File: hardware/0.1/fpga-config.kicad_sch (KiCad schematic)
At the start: 31 parts, among them J2 JTAG, J5 USB_C_Receptacle_USB2.0, Q1 BSS138, SW1 SW_Push, U1 ECP5U_12_CABGA256, U4 USBLC6-2SC6, U6 W25Q128JVSIQ

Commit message: all DRC / ERC errors signed off
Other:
- note added: "Enables bootloader to reset into user land. DNP until bootloader development begins."
- note added: "IO / configure to jump to bootloader"
- note removed: "Can be used for IO or to jump to bootloader"
- note removed: "Self reboot system? DNP until I figure out what goes on."
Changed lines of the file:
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@@
   (page 3 5)
   (paper "A4")
+  (bus_alias "CONFIG" (members "CFG_CLK" "CFG_IO[0..3]" "CFG_CDONE" "CFG_CS"))
   (junction (at 27.305 74.93) (diameter 1.016) (color 0 0 0 0))
+  (junction (at 46.99 35.56) (diameter 1.016) (color 0 0 0 0))
   (junction (at 47.625 49.53) (diameter 1.016) (color 0 0 0 0))
   (junction (at 47.625 54.61) (diameter 1.016) (color 0 0 0 0))
@@
   (junction (at 269.24 57.15) (diameter 1.016) (color 0 0 0 0))
   (junction (at 269.24 71.12) (diameter 1.016) (color 0 0 0 0))
-  (no_connect (at 229.87 111.76))
-  (no_connect (at 46.355 66.04))
-  (no_connect (at 229.87 144.78))
-  (no_connect (at 46.355 63.5))
+  (no_connect (at 229.87 121.92))
   (no_connect (at 229.87 119.38))
   (no_connect (at 229.87 114.3))
   (no_connect (at 229.87 116.84))
+  (no_connect (at 46.355 63.5))
+  (no_connect (at 229.87 111.76))
+  (no_connect (at 46.355 66.04))
   (no_connect (at 229.87 137.16))
-  (no_connect (at 229.87 121.92))
+  (no_connect (at 229.87 144.78))
   (bus_entry (at 114.935 49.53) (size 2.54 -2.54)
     (stroke (width 0.1524) (type solid) (color 0 0 0 0))
@@
     (stroke (width 0) (type solid) (color 0 0 0 0))
   )
-  (wire (pts (xy 46.355 35.56) (xy 48.895 35.56))
+  (wire (pts (xy 46.355 35.56) (xy 46.99 35.56))
     (stroke (width 0) (type solid) (color 0 0 0 0))
   )
@@
   )
   (wire (pts (xy 46.355 55.88) (xy 47.625 55.88))
+    (stroke (width 0) (type solid) (color 0 0 0 0))
+  )
+  (wire (pts (xy 46.99 30.48) (xy 46.99 35.56))
+    (stroke (width 0) (type solid) (color 0 0 0 0))
+  )
+  (wire (pts (xy 46.99 35.56) (xy 48.895 35.56))
     (stroke (width 0) (type solid) (color 0 0 0 0))
   )
@@
     (effects (font (size 5 5)) (justify right bottom))
   )
-  (text "Can be used for IO or\nto jump to bootloader" (at 162.56 153.67 180)
+  (text "IO / configure to \njump to bootloader" (at 162.56 153.67 180)
     (effects (font (size 1.27 1.27)) (justify right bottom))
   )
@@
     (effects (font (size 1.27 1.27)) (justify left bottom))
   )
-  (text "Self reboot system?\nDNP until I figure out what goes on."
-    (at 198.12 153.67 0)
+  (text "Enables bootloader to reset into user land.\nDNP until bootloader development begins."
+    (at 200.66 154.94 0)
     (effects (font (size 1.27 1.27)) (justify left bottom))
   )
@@
     (effects (font (size 1.27 1.27)) (justify left bottom))
   )
+  (label "{CONFIG}" (at 215.9 45.72 270)
+    (effects (font (size 1.27 1.27)) (justify right bottom))
+  )
   (label "CFG_CLK" (at 218.44 99.06 0)
     (effects (font (size 1.27 1.27)) (justify left bottom))
@@
     (effects (font (size 1.27 1.27)) (justify left))
   )
+  (symbol (lib_id "power:PWR_FLAG") (at 46.99 30.48 0) (unit 1)
+    (in_bom yes) (on_board yes)
+    (property "Reference" "#FLG0105" (id 0) (at 46.99 28.575 0)
+      (effects (font (size 1.27 1.27)) hide)
+    )
+    (property "Value" "PWR_FLAG" (id 1) (at 46.99 26.67 0))
+    (property "Footprint" "" (id 2) (at 46.99 30.48 0)
+      (effects (font (size 1.27 1.27)) hide)
+    )
+    (property "Datasheet" "~" (id 3) (at 46.99 30.48 0)
+      (effects (font (size 1.27 1.27)) hide)
+    )
+  )
   (symbol (lib_id "power:+3V3") (at 24.13 97.79 0) (mirror y) (unit 1)

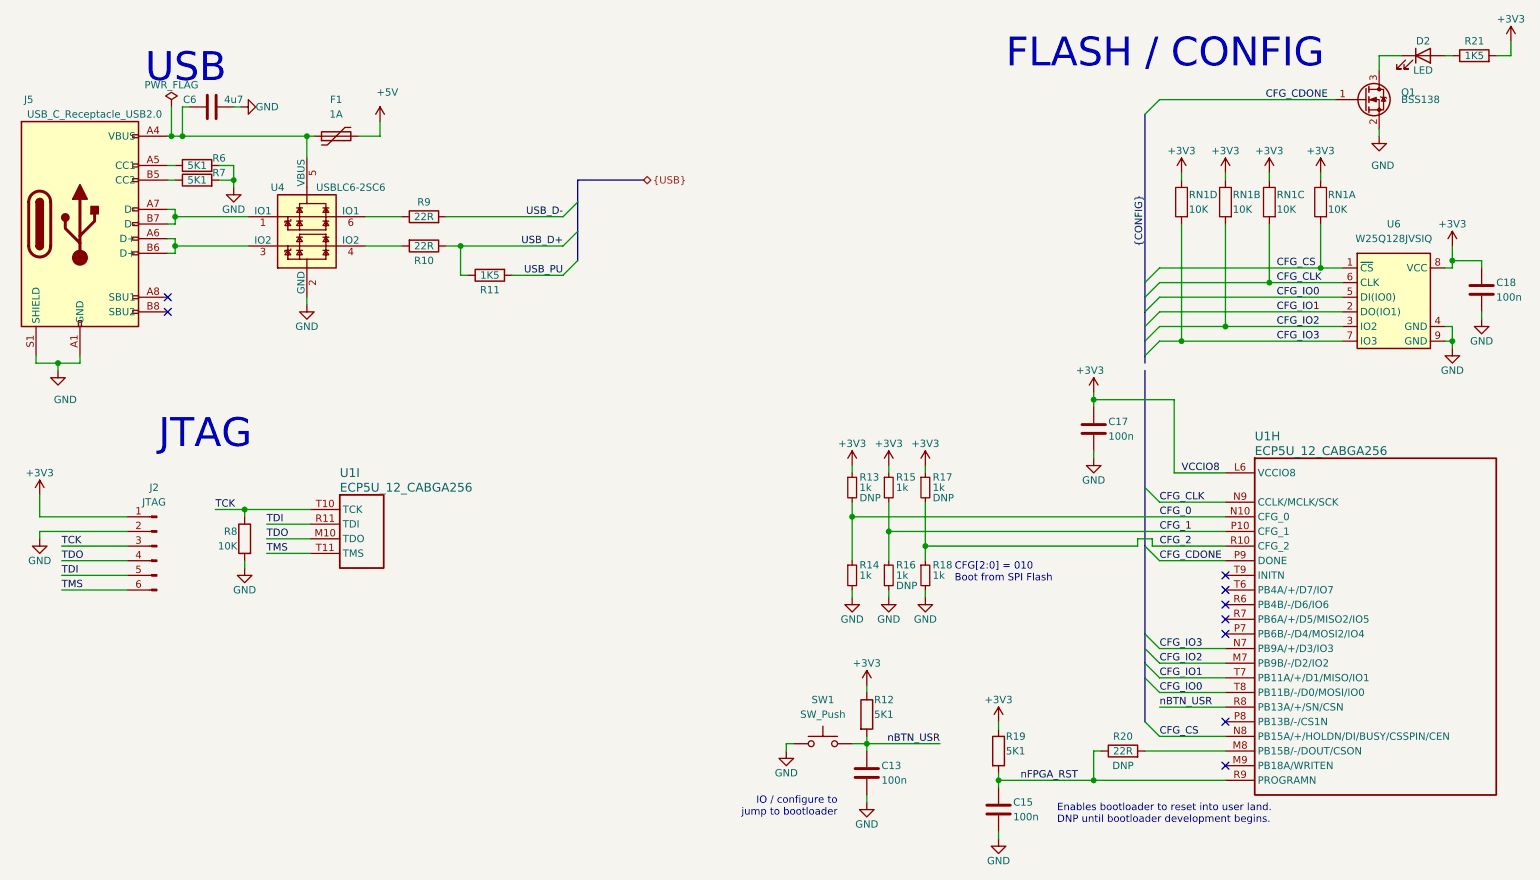
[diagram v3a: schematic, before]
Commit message: adding silk
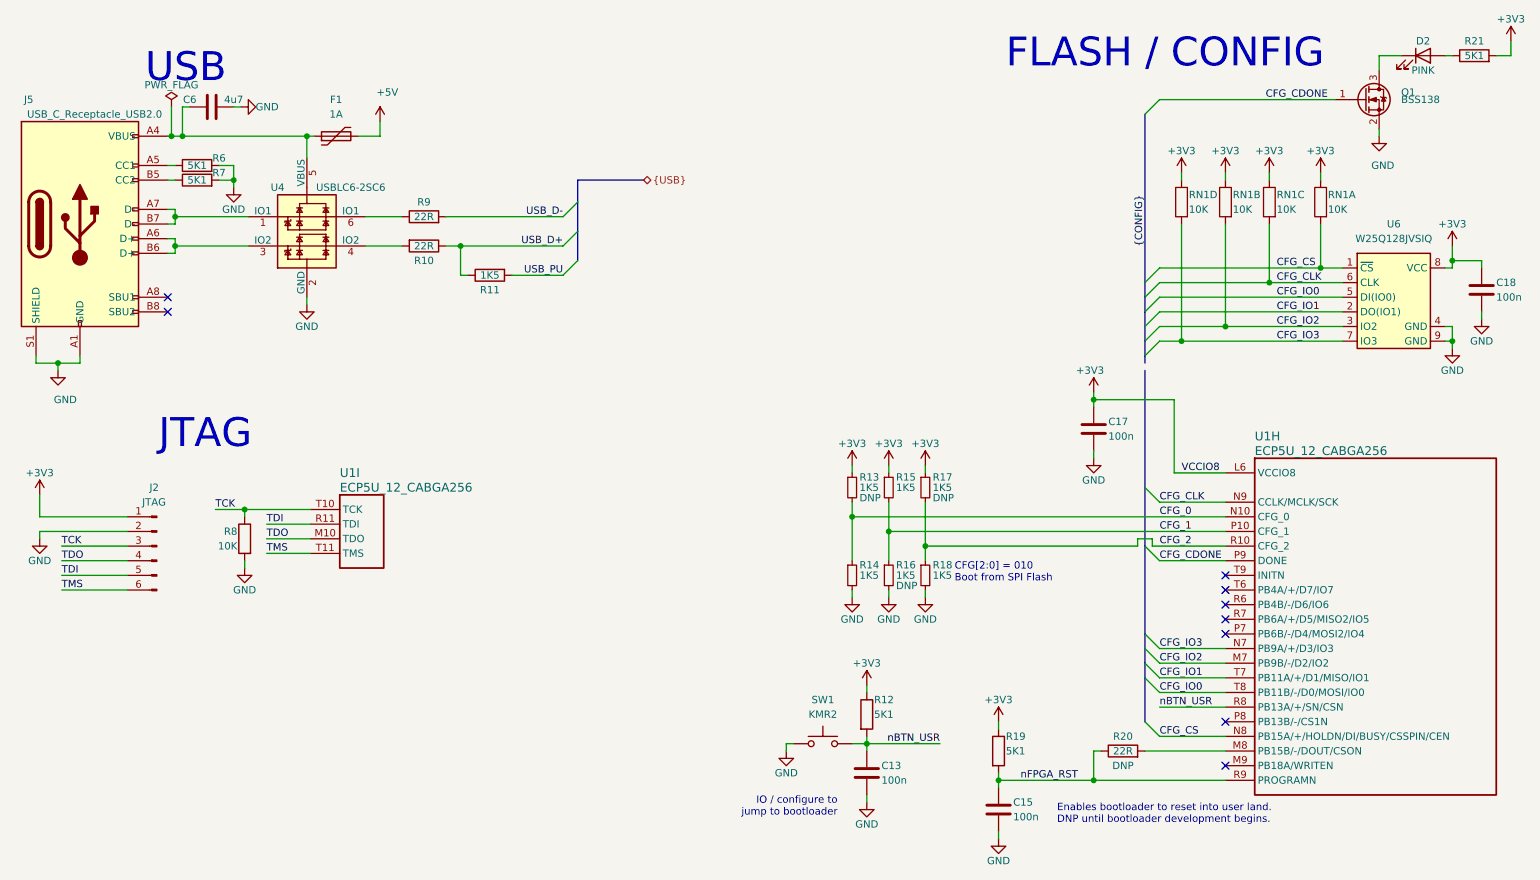
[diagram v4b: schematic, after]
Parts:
- D2: value LED -> PINK
- J2: DNP (none) -> DNP
- R13, R14, R15, R16, R17, R18: value 1k -> 1K5
- R21: value 1K5 -> 5K1
- SW1: value SW_Push -> KMR2
- U1: manf# ECP5U_12 -> (none)
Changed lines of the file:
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@@
   (junction (at 269.24 57.15) (diameter 1.016) (color 0 0 0 0))
   (junction (at 269.24 71.12) (diameter 1.016) (color 0 0 0 0))
+  (no_connect (at 229.87 121.92))
   (no_connect (at 229.87 111.76))
-  (no_connect (at 229.87 121.92))
-  (no_connect (at 229.87 116.84))
+  (no_connect (at 229.87 144.78))
   (no_connect (at 46.355 63.5))
   (no_connect (at 229.87 114.3))
+  (no_connect (at 229.87 119.38))
+  (no_connect (at 229.87 116.84))
+  (no_connect (at 46.355 66.04))
   (no_connect (at 229.87 137.16))
-  (no_connect (at 229.87 144.78))
-  (no_connect (at 46.355 66.04))
-  (no_connect (at 229.87 119.38))
   (bus_entry (at 114.935 49.53) (size 2.54 -2.54)
     (stroke (width 0.1524) (type solid) (color 0 0 0 0))
@@
       (effects (font (size 1.27 1.27)) (justify left top))
     )
-    (property "Value" "1k" (id 1) (at 166.37 96.52 0)
+    (property "Value" "1K5" (id 1) (at 166.37 96.52 0)
       (effects (font (size 1.27 1.27)) (justify left))
     )
@@
       (effects (font (size 1.27 1.27)) (justify left top))
     )
-    (property "Value" "1k" (id 1) (at 166.37 111.76 0)
+    (property "Value" "1K5" (id 1) (at 166.37 111.76 0)
       (effects (font (size 1.27 1.27)) (justify left))
     )
@@
       (effects (font (size 1.27 1.27)) (justify left top))
     )
-    (property "Value" "1k" (id 1) (at 172.72 96.52 0)
+    (property "Value" "1K5" (id 1) (at 172.72 96.52 0)
       (effects (font (size 1.27 1.27)) (justify left))
     )
@@
       (effects (font (size 1.27 1.27)) (justify left top))
     )
-    (property "Value" "1k" (id 1) (at 172.72 111.76 0)
+    (property "Value" "1K5" (id 1) (at 172.72 111.76 0)
       (effects (font (size 1.27 1.27)) (justify left))
     )
@@
       (effects (font (size 1.27 1.27)) (justify left top))
     )
-    (property "Value" "1k" (id 1) (at 179.07 96.52 0)
+    (property "Value" "1K5" (id 1) (at 179.07 96.52 0)
       (effects (font (size 1.27 1.27)) (justify left))
     )
@@
       (effects (font (size 1.27 1.27)) (justify left top))
     )
-    (property "Value" "1k" (id 1) (at 179.07 111.76 0)
+    (property "Value" "1K5" (id 1) (at 179.07 111.76 0)
       (effects (font (size 1.27 1.27)) (justify left))
     )
@@
     (in_bom yes) (on_board yes)
     (property "Reference" "R21" (id 0) (at 273.05 19.05 90))
-    (property "Value" "1K5" (id 1) (at 273.05 21.59 90))
+    (property "Value" "5K1" (id 1) (at 273.05 21.59 90))
     (property "Footprint" "Resistor_SMD:R_0402_1005Metric" (id 2) (at 273.05 23.368 90)
       (effects (font (size 1.27 1.27)) hide)
@@
     (in_bom yes) (on_board yes)
     (property "Reference" "D2" (id 0) (at 264.16 19.05 0))
-    (property "Value" "LED" (id 1) (at 264.16 24.13 0))
+    (property "Value" "PINK" (id 1) (at 264.16 24.13 0))
     (property "Footprint" "LED_SMD:LED_0603_1608Metric" (id 2) (at 264.16 21.59 0)
       (effects (font (size 1.27 1.27)) hide)
@@
     (in_bom yes) (on_board yes)
     (property "Reference" "SW1" (id 0) (at 160.02 133.35 0))
-    (property "Value" "SW_Push" (id 1) (at 160.02 135.89 0))
+    (property "Value" "KMR2" (id 1) (at 160.02 135.89 0))
     (property "Footprint" "josh-buttons-switches:SW_Push_KMR2" (id 2) (at 160.02 135.89 0)
       (effects (font (size 1.27 1.27)) hide)
@@
       (effects (font (size 1.27 1.27)) hide)
     )
+    (property "DNP" "DNP" (id 4) (at 44.45 106.68 0)
+      (effects (font (size 1.27 1.27)) hide)
+    )
   )
   (symbol (lib_id "Transistor_FET:BSS138") (at 254 29.21 0) (unit 1)
@@
       (effects (font (size 1.27 1.27) italic) (justify left) hide)
     )
-    (property "Datasheet" "https://www.onsemi.com/pub/Collateral/BSS138-D.PDF" (id 3) (at 254 29.21 0)
+    (property "Datasheet" "" (id 3) (at 254 29.21 0)
       (effects (font (size 1.27 1.27)) (justify left) hide)
     )
@@
       (effects (font (size 1.524 1.524)) (justify right) hide)
     )
-    (property "manf#" "ECP5U_12" (id 4) (at 86.36 58.42 0)
+    (property "manf#" "" (id 4) (at 86.36 58.42 0)
       (effects (font (size 1.524 1.524)) (justify right) hide)
     )
@@
       (effects (font (size 1.27 1.27)) hide)
     )
-    (property "Datasheet" "http://www.winbond.com/resource-files/w25q32jv%20revg%2003272018%20plus.pdf" (id 3) (at 262.89 63.5 0)
+    (property "Datasheet" "" (id 3) (at 262.89 63.5 0)
       (effects (font (size 1.27 1.27)) hide)
     )
@@
       (effects (font (size 1.27 1.27)) hide)
     )
-    (property "Datasheet" "http://www2.st.com/resource/en/datasheet/CD00050750.pdf" (id 3) (at 75.565 43.18 0)
+    (property "Datasheet" "" (id 3) (at 75.565 43.18 0)
       (effects (font (size 1.27 1.27)) hide)
     )
@@
       (effects (font (size 1.27 1.27)) hide)
     )
-    (property "Datasheet" "https://www.usb.org/sites/default/files/documents/usb_type-c.zip" (id 3) (at 34.925 50.8 0)
+    (property "Datasheet" "" (id 3) (at 34.925 50.8 0)
       (effects (font (size 1.27 1.27)) hide)
     )
@@
       (effects (font (size 1.524 1.524)) (justify right) hide)
     )
-    (property "manf#" "ECP5U_12" (id 4) (at 259.08 86.36 0)
+    (property "manf#" "" (id 4) (at 259.08 86.36 0)
       (effects (font (size 1.524 1.524)) (justify right) hide)
     )
